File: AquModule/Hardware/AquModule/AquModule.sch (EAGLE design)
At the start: 1 part

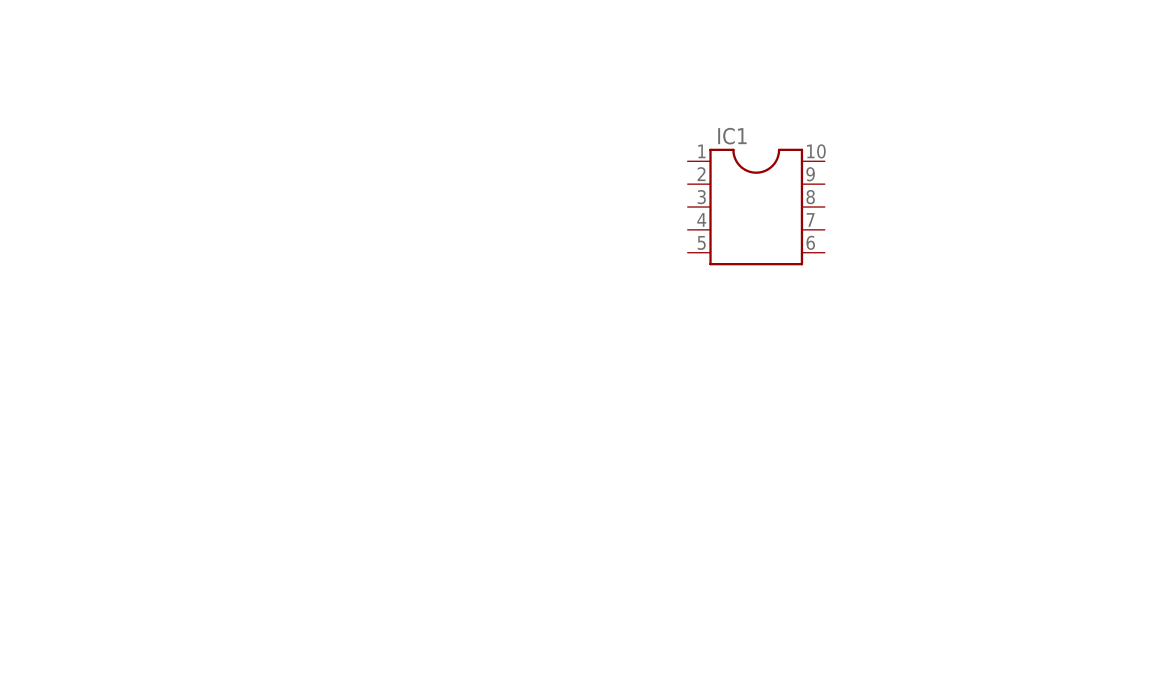
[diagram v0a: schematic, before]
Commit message: Wired all the components and made first PCB wiring
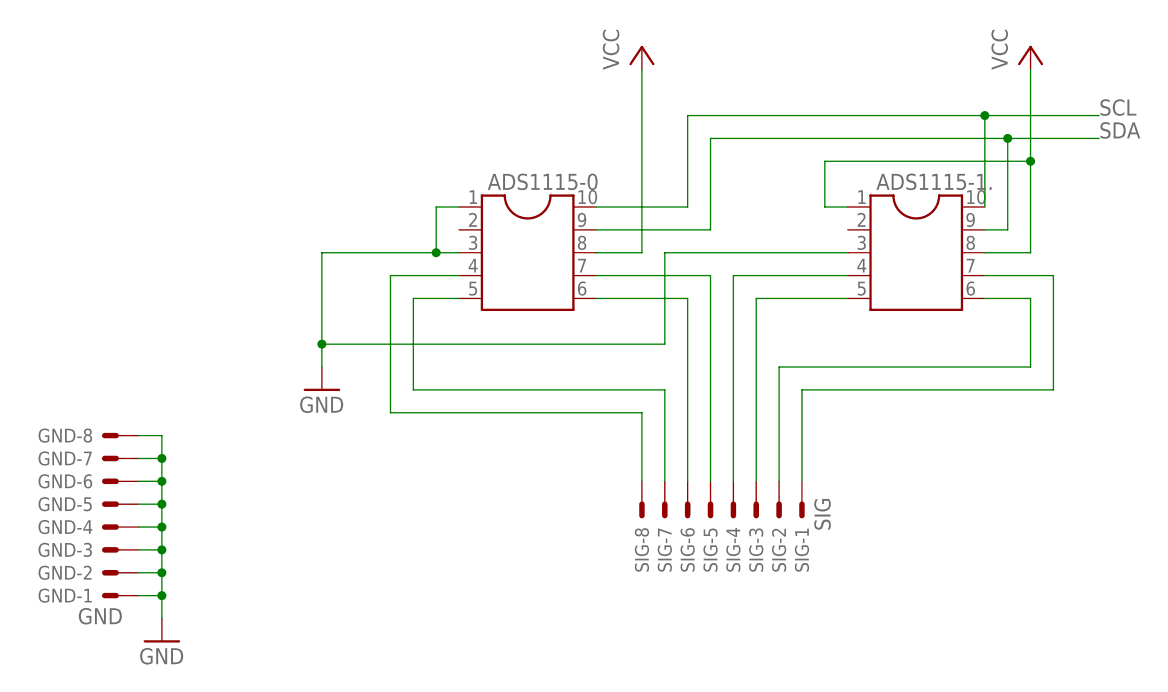
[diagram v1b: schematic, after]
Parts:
- removed IC1: (no value), ic-package:DIL10
- added ADS1115-0, ADS1115-1.: (no value), ic-package:DIL10
- added GND: GND, con-molex:C-GRID-08-15-91
- added SIG: SIG, con-molex:C-GRID-08-15-91
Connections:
- new net GND: ADS1115-0.1, ADS1115-0.3, ADS1115-1..3, GND-1.S, GND-2.S, GND-3.S, GND-4.S, GND-5.S, GND-6.S, GND-7.S, GND-8.S
- new net N$1: ADS1115-0.4, SIG-8.S
- new net N$2: ADS1115-0.5, SIG-7.S
- new net N$3: ADS1115-0.6, SIG-6.S
- new net N$4: ADS1115-0.7, SIG-5.S
- new net N$5: ADS1115-1..4, SIG-4.S
- new net N$6: ADS1115-1..5, SIG-3.S
- new net N$7: ADS1115-1..6, SIG-2.S
- new net N$8: ADS1115-1..7, SIG-1.S
- new net SCL: ADS1115-0.10, ADS1115-1..10
- new net SDA: ADS1115-0.9, ADS1115-1..9
- new net VCC: ADS1115-0.8, ADS1115-1..1, ADS1115-1..8

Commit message: PCB design for module 1 - Ready
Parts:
- added C1, C2, C3, C4, C5, C6, C7, C8: 100nF, rcl:C-EUC1005
- added POW_LED: LS_T679-D2E2-1, led:LS_T679-D2E2-1
- added R1, R2, R3, R4, R5, R6, R7, R8: 1K, resistor:R-EU_R0603
- added R9: ?, resistor:R-EU_0207/2V
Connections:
- new net N$10: R2.1, SIG-7.S
- new net N$11: R3.1, SIG-6.S
- new net N$12: R4.1, SIG-5.S
- new net N$13: R5.1, SIG-4.S
- new net N$14: R6.1, SIG-3.S
- new net N$15: R7.1, SIG-2.S
- new net N$16: R8.1, SIG-1.S
- new net N$17: POW_LED.C, R9.2
- new net N$9: R1.1, SIG-8.S
- net GND: now also C1.1, C2.1, C3.1, C4.1, C5.1, C6.1, C7.1, C8.1, R9.1
- net N$1: now also C8.2, R1.2; no longer SIG-8.S
- net N$2: now also C7.2, R2.2; no longer SIG-7.S
- net N$3: now also C6.2, R3.2; no longer SIG-6.S
- net N$4: now also C5.2, R4.2; no longer SIG-5.S
- net N$5: now also C4.2, R5.2; no longer SIG-4.S
- net N$6: now also C3.2, R6.2; no longer SIG-3.S
- net N$7: now also C2.2, R7.2; no longer SIG-2.S
- net N$8: now also C1.2, R8.2; no longer SIG-1.S
- net VCC: now also POW_LED.A
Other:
- moved on the sheet: ADS1115-0, ADS1115-1., GND-1, GND-2, GND-3, GND-4, GND-5, GND-6, GND-7, GND-8, SIG-1, SIG-2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

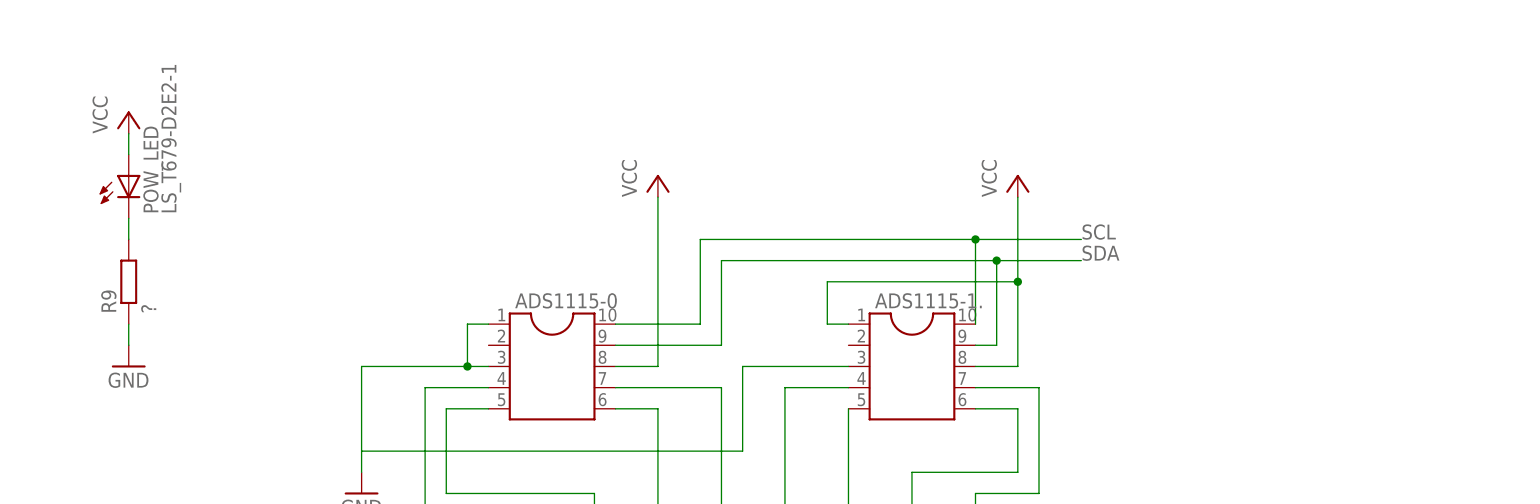
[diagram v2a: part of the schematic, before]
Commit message: PCB ADD0 and ADD1 ready
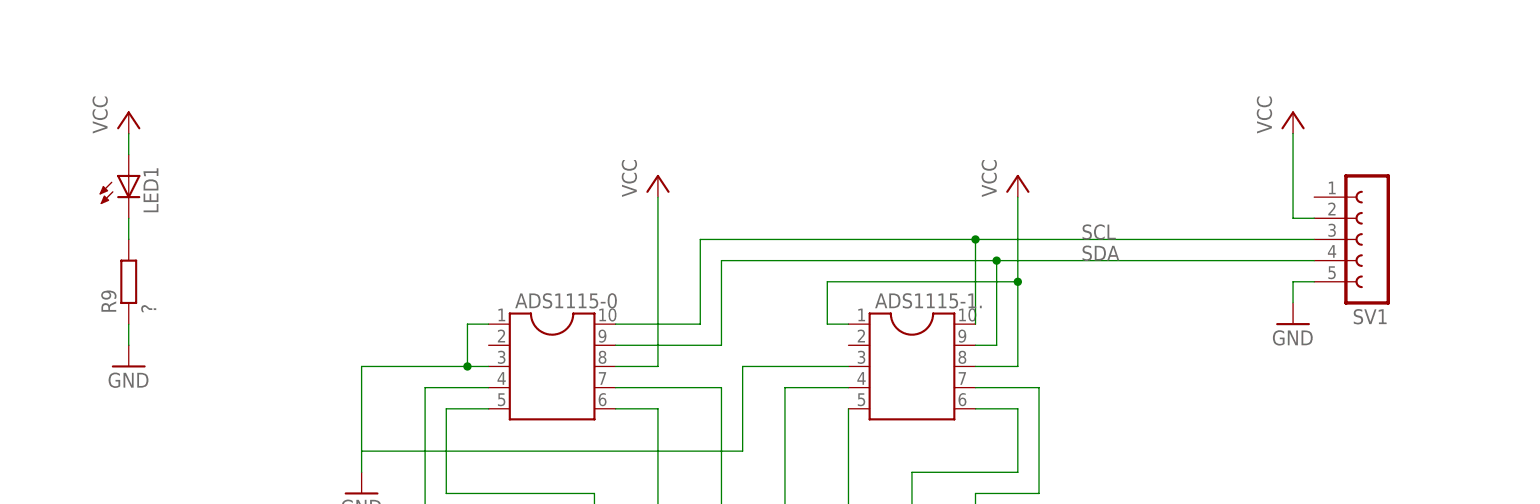
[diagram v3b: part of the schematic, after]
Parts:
- removed POW_LED: LS_T679-D2E2-1, led:LS_T679-D2E2-1
- added LED1: (no value), eagle-ltspice:LED_ELD260
- added SV1: (no value), con-lsta:FE05-1
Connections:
- net GND: now also SV1.5
- net N$17: now also LED1.C; no longer POW_LED.C
- net SCL: now also SV1.3
- net SDA: now also SV1.4
- net VCC: now also LED1.A, SV1.2; no longer POW_LED.A
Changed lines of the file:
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@@
 <layer number="97" name="Info" color="7" fill="1" visible="yes" active="yes"/>
 <layer number="98" name="Guide" color="6" fill="1" visible="yes" active="yes"/>
+<layer number="99" name="SpiceOrder" color="5" fill="1" visible="yes" active="yes"/>
 </layers>
 <schematic xreflabel="%F%N/%S.%C%R" xrefpart="/%S.%C%R">
@@
 <part name="GND9" library="supply1" deviceset="GND" device=""/>
 <part name="GND10" library="supply1" deviceset="GND" device=""/>
-<part name="POW_LED" library="led" deviceset="*_T679-?-1" device="D2E2" technology="LS"/>
 <part name="GND11" library="supply1" deviceset="GND" device=""/>
 <part name="P+3" library="supply1" deviceset="VCC" device=""/>
 <part name="R9" library="resistor" deviceset="R-EU_" device="0207/2V" value="?"/>
+<part name="SV1" library="con-lsta" deviceset="FE05-1" device=""/>
+<part name="GND12" library="supply1" deviceset="GND" device=""/>
+<part name="P+4" library="supply1" deviceset="VCC" device=""/>
+<part name="LED1" library="eagle-ltspice" deviceset="LED_E" device="LD260"/>
 </parts>
 <sheets>
@@
 <instance part="GND9" gate="1" x="172.72" y="71.12"/>
 <instance part="GND10" gate="1" x="162.56" y="68.58"/>
-<instance part="POW_LED" gate="G$1" x="40.64" y="144.78"/>
 <instance part="GND11" gate="1" x="40.64" y="121.92"/>
 <instance part="P+3" gate="VCC" x="40.64" y="152.4"/>
 <instance part="R9" gate="G$1" x="40.64" y="132.08" rot="R90"/>
+<instance part="SV1" gate="G$1" x="190.5" y="137.16" rot="R180"/>
+<instance part="GND12" gate="1" x="180.34" y="127"/>
+<instance part="P+4" gate="VCC" x="180.34" y="152.4"/>
+<instance part="LED1" gate="G$1" x="40.64" y="144.78"/>
 </instances>
 <busses>
@@
 <wire x1="40.64" y1="127" x2="40.64" y2="124.46" width="0.1524" layer="91"/>
 </segment>
+<segment>
+<pinref part="SV1" gate="G$1" pin="5"/>
+<pinref part="GND12" gate="1" pin="GND"/>
+<wire x1="182.88" y1="132.08" x2="180.34" y2="132.08" width="0.1524" layer="91"/>
+<wire x1="180.34" y1="132.08" x2="180.34" y2="129.54" width="0.1524" layer="91"/>
+</segment>
 </net>
 <net name="VCC" class="0">
@@
 <segment>
 <pinref part="P+3" gate="VCC" pin="VCC"/>
-<pinref part="POW_LED" gate="G$1" pin="A"/>
 <wire x1="40.64" y1="149.86" x2="40.64" y2="147.32" width="0.1524" layer="91"/>
+<pinref part="LED1" gate="G$1" pin="A"/>
+</segment>
+<segment>
+<pinref part="P+4" gate="VCC" pin="VCC"/>
+<wire x1="180.34" y1="149.86" x2="180.34" y2="139.7" width="0.1524" layer="91"/>
+<pinref part="SV1" gate="G$1" pin="2"/>
+<wire x1="180.34" y1="139.7" x2="182.88" y2="139.7" width="0.1524" layer="91"/>
 </segment>
 </net>
@@
 <label x="154.94" y="137.16" size="1.778" layer="95"/>
 <pinref part="ADS1115-1." gate="G$1" pin="10"/>
-<wire x1="142.24" y1="137.16" x2="154.94" y2="137.16" width="0.1524" layer="91"/>
 <wire x1="142.24" y1="127" x2="142.24" y2="137.16" width="0.1524" layer="91"/>
 <junction x="142.24" y="137.16"/>
+<pinref part="SV1" gate="G$1" pin="3"/>
+<wire x1="142.24" y1="137.16" x2="182.88" y2="137.16" width="0.1524" layer="91"/>
 </segment>
 </net>
@@
 <wire x1="111.76" y1="134.62" x2="144.78" y2="134.62" width="0.1524" layer="91"/>
 <pinref part="ADS1115-1." gate="G$1" pin="9"/>
-<wire x1="144.78" y1="134.62" x2="154.94" y2="134.62" width="0.1524" layer="91"/>
 <wire x1="142.24" y1="124.46" x2="144.78" y2="124.46" width="0.1524" layer="91"/>
 <wire x1="144.78" y1="124.46" x2="144.78" y2="134.62" width="0.1524" layer="91"/>
 <junction x="144.78" y="134.62"/>
 <label x="154.94" y="134.62" size="1.778" layer="95"/>
+<wire x1="144.78" y1="134.62" x2="182.88" y2="134.62" width="0.1524" layer="91"/>
+<pinref part="SV1" gate="G$1" pin="4"/>
 </segment>
 </net>
@@
 <net name="N$17" class="0">
 <segment>
-<pinref part="POW_LED" gate="G$1" pin="C"/>
 <pinref part="R9" gate="G$1" pin="2"/>
 <wire x1="40.64" y1="139.7" x2="40.64" y2="137.16" width="0.1524" layer="91"/>
-</segment>
-</net>
+<pinref part="LED1" gate="G$1" pin="C"/>
+</segment>
+</net>

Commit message: Aqu Module 2 PCB - Ready
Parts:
- LED1: value (none) -> GREEN
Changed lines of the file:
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@@
 <grid distance="0.1" unitdist="inch" unit="inch" style="lines" multiple="1" display="no" altdistance="0.01" altunitdist="inch" altunit="inch"/>
 <layers>
-<layer number="1" name="Top" color="4" fill="1" visible="yes" active="no"/>
-<layer number="2" name="Route2" color="1" fill="3" visible="yes" active="no"/>
-<layer number="3" name="Route3" color="4" fill="3" visible="yes" active="no"/>
-<layer number="4" name="Route4" color="1" fill="4" visible="yes" active="no"/>
-<layer number="5" name="Route5" color="4" fill="4" visible="yes" active="no"/>
-<layer number="6" name="Route6" color="1" fill="8" visible="yes" active="no"/>
-<layer number="7" name="Route7" color="4" fill="8" visible="yes" active="no"/>
-<layer number="8" name="Route8" color="1" fill="2" visible="yes" active="no"/>
-<layer number="9" name="Route9" color="4" fill="2" visible="yes" active="no"/>
-<layer number="10" name="Route10" color="1" fill="7" visible="yes" active="no"/>
-<layer number="11" name="Route11" color="4" fill="7" visible="yes" active="no"/>
-<layer number="12" name="Route12" color="1" fill="5" visible="yes" active="no"/>
-<layer number="13" name="Route13" color="4" fill="5" visible="yes" active="no"/>
-<layer number="14" name="Route14" color="1" fill="6" visible="yes" active="no"/>
-<layer number="15" name="Route15" color="4" fill="6" visible="yes" active="no"/>
-<layer number="16" name="Bottom" color="1" fill="1" visible="yes" active="no"/>
-<layer number="17" name="Pads" color="2" fill="1" visible="yes" active="no"/>
-<layer number="18" name="Vias" color="2" fill="1" visible="yes" active="no"/>
-<layer number="19" name="Unrouted" color="6" fill="1" visible="yes" active="no"/>
-<layer number="20" name="Dimension" color="15" fill="1" visible="yes" active="no"/>
-<layer number="21" name="tPlace" color="7" fill="1" visible="yes" active="no"/>
-<layer number="22" name="bPlace" color="7" fill="1" visible="yes" active="no"/>
-<layer number="23" name="tOrigins" color="15" fill="1" visible="yes" active="no"/>
-<layer number="24" name="bOrigins" color="15" fill="1" visible="yes" active="no"/>
-<layer number="25" name="tNames" color="7" fill="1" visible="yes" active="no"/>
-<layer number="26" name="bNames" color="7" fill="1" visible="yes" active="no"/>
-<layer number="27" name="tValues" color="7" fill="1" visible="yes" active="no"/>
-<layer number="28" name="bValues" color="7" fill="1" visible="yes" active="no"/>
+<layer number="1" name="Top" color="4" fill="1" visible="no" active="no"/>
+<layer number="2" name="Route2" color="1" fill="3" visible="no" active="no"/>
+<layer number="3" name="Route3" color="4" fill="3" visible="no" active="no"/>
+<layer number="4" name="Route4" color="1" fill="4" visible="no" active="no"/>
+<layer number="5" name="Route5" color="4" fill="4" visible="no" active="no"/>
+<layer number="6" name="Route6" color="1" fill="8" visible="no" active="no"/>
+<layer number="7" name="Route7" color="4" fill="8" visible="no" active="no"/>
+<layer number="8" name="Route8" color="1" fill="2" visible="no" active="no"/>
+<layer number="9" name="Route9" color="4" fill="2" visible="no" active="no"/>
+<layer number="10" name="Route10" color="1" fill="7" visible="no" active="no"/>
+<layer number="11" name="Route11" color="4" fill="7" visible="no" active="no"/>
+<layer number="12" name="Route12" color="1" fill="5" visible="no" active="no"/>
+<layer number="13" name="Route13" color="4" fill="5" visible="no" active="no"/>
+<layer number="14" name="Route14" color="1" fill="6" visible="no" active="no"/>
+<layer number="15" name="Route15" color="4" fill="6" visible="no" active="no"/>
+<layer number="16" name="Bottom" color="1" fill="1" visible="no" active="no"/>
+<layer number="17" name="Pads" color="2" fill="1" visible="no" active="no"/>
+<layer number="18" name="Vias" color="2" fill="1" visible="no" active="no"/>
+<layer number="19" name="Unrouted" color="6" fill="1" visible="no" active="no"/>
+<layer number="20" name="Dimension" color="15" fill="1" visible="no" active="no"/>
+<layer number="21" name="tPlace" color="7" fill="1" visible="no" active="no"/>
+<layer number="22" name="bPlace" color="7" fill="1" visible="no" active="no"/>
+<layer number="23" name="tOrigins" color="15" fill="1" visible="no" active="no"/>
+<layer number="24" name="bOrigins" color="15" fill="1" visible="no" active="no"/>
+<layer number="25" name="tNames" color="7" fill="1" visible="no" active="no"/>
+<layer number="26" name="bNames" color="7" fill="1" visible="no" active="no"/>
+<layer number="27" name="tValues" color="7" fill="1" visible="no" active="no"/>
+<layer number="28" name="bValues" color="7" fill="1" visible="no" active="no"/>
 <layer number="29" name="tStop" color="7" fill="3" visible="no" active="no"/>
 <layer number="30" name="bStop" color="7" fill="6" visible="no" active="no"/>
@@
 <layer number="35" name="tGlue" color="7" fill="4" visible="no" active="no"/>
 <layer number="36" name="bGlue" color="7" fill="5" visible="no" active="no"/>
-<layer number="37" name="tTest" color="7" fill="1" visible="yes" active="no"/>
-<layer number="38" name="bTest" color="7" fill="1" visible="yes" active="no"/>
+<layer number="37" name="tTest" color="7" fill="1" visible="no" active="no"/>
+<layer number="38" name="bTest" color="7" fill="1" visible="no" active="no"/>
 <layer number="39" name="tKeepout" color="4" fill="11" visible="no" active="no"/>
 <layer number="40" name="bKeepout" color="1" fill="11" visible="no" active="no"/>
@@
 <layer number="44" name="Drills" color="7" fill="1" visible="no" active="no"/>
 <layer number="45" name="Holes" color="7" fill="1" visible="no" active="no"/>
-<layer number="46" name="Milling" color="3" fill="1" visible="yes" active="no"/>
-<layer number="47" name="Measures" color="7" fill="1" visible="yes" active="no"/>
-<layer number="48" name="Document" color="7" fill="1" visible="yes" active="no"/>
-<layer number="49" name="Reference" color="7" fill="1" visible="yes" active="no"/>
-<layer number="51" name="tDocu" color="7" fill="1" visible="yes" active="no"/>
-<layer number="52" name="bDocu" color="7" fill="1" visible="yes" active="no"/>
+<layer number="46" name="Milling" color="3" fill="1" visible="no" active="no"/>
+<layer number="47" name="Measures" color="7" fill="1" visible="no" active="no"/>
+<layer number="48" name="Document" color="7" fill="1" visible="no" active="no"/>
+<layer number="49" name="Reference" color="7" fill="1" visible="no" active="no"/>
+<layer number="51" name="tDocu" color="7" fill="1" visible="no" active="no"/>
+<layer number="52" name="bDocu" color="7" fill="1" visible="no" active="no"/>
 <layer number="91" name="Nets" color="2" fill="1" visible="yes" active="yes"/>
 <layer number="92" name="Busses" color="1" fill="1" visible="yes" active="yes"/>
@@
 <part name="GND12" library="supply1" deviceset="GND" device=""/>
 <part name="P+4" library="supply1" deviceset="VCC" device=""/>
-<part name="LED1" library="eagle-ltspice" deviceset="LED_E" device="LD260"/>
+<part name="LED1" library="eagle-ltspice" deviceset="LED_E" device="LD260" value="GREEN"/>
 </parts>
 <sheets>
